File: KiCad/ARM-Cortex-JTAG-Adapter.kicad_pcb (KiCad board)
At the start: 2 copper layers, 36.1 x 30.5 mm, 5 parts, among them J1 Data, J2 Power

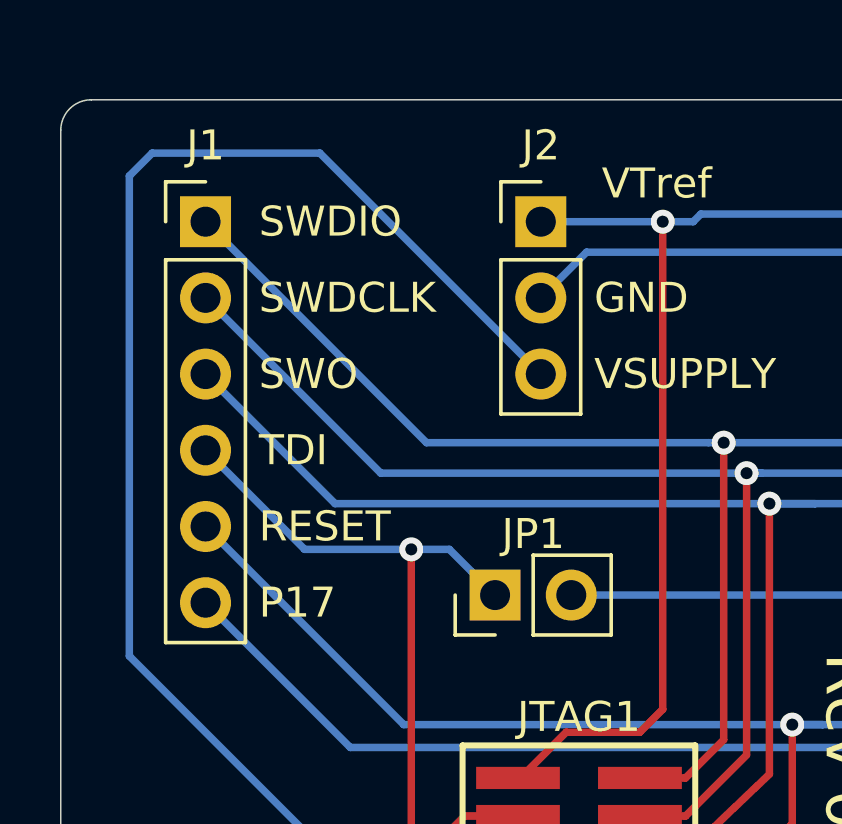
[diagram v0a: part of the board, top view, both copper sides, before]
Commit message: Redoing footprints and symbols.
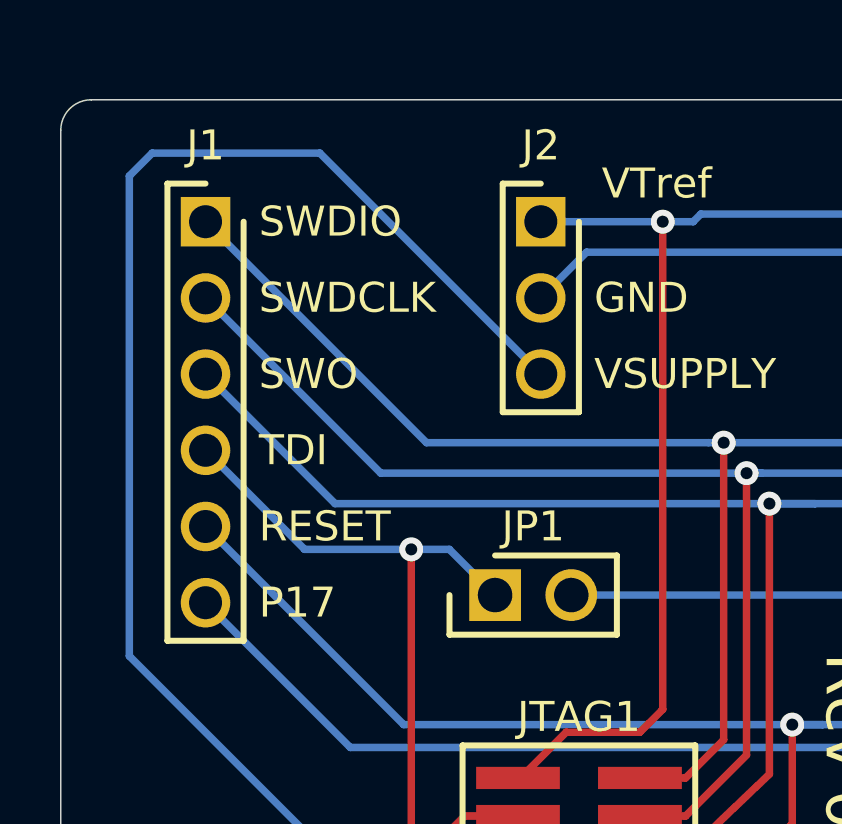
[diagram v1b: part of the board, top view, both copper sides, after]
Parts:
- H1: value 200-SSW11002TDRA -> SSW-110-02-T-D-RA
- J1: value Data -> M20-9990646; footprint Connector_PinHeader_2.54mm:PinHeader_1x06_P2.54mm_Vertical -> (Local):m20-9990646
- J2: value Power -> M20-9990346; footprint Connector_PinHeader_2.54mm:PinHeader_1x03_P2.54mm_Vertical -> (Local):m20-9990346
- JP1: value 855-M50-3530342 -> M20-9990246; footprint Connector_PinHeader_2.54mm:PinHeader_1x02_P2.54mm_Vertical -> (Local):M20-9990246
- turned J1 to 270 degrees
- turned J2 to 270 degrees
- turned JP1 to 0 degrees
